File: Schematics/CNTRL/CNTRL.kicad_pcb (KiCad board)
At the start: 4 copper layers, 78 x 78 mm, 128 parts, among them J1 SWD, J10 Y+, J11 Y-, J12 693071020811, J13 3.3V, J14 NAV I2C, J15 I2C, J16 USART, J17 PYRO1_OSTTE020104, J18 PYRO3_OSTTE020104, J19 USB_A_TE_292303-7_Horizontal, J2 CONSMA001-SMD-G-T, J20 PYRO2_OSTTE020104, J21 PYRO4_OSTTE020104, J3 3S LiPo, J4 F4, J5 F3, J6 F2, J7 F1, J8 X+, J9 X-, Q1 BUK9832-55A_CUX, Q2 BUK9832-55A_CUX, Q3 BUK9832-55A_CUX, Q4 BUK9832-55A_CUX, Q5 MMBT2222A-TP, SW1 OS102011MS2QN1, SW2 Omron_B3F-10xx, U1 STM32405RGT6, U2 RFM95W-915S2, U3 TPS2117DRLR, U4 TPS563200, U5 AMS1117-3.3, U6 AMS1117-5.0, U7 W25Q128JVSIQ, U8 USBLC6-2SC6, Y1 12MHz_ECS-120-18-33-JGN-TR3, Y2 32.768KHz_SC32S-7PF20PPM

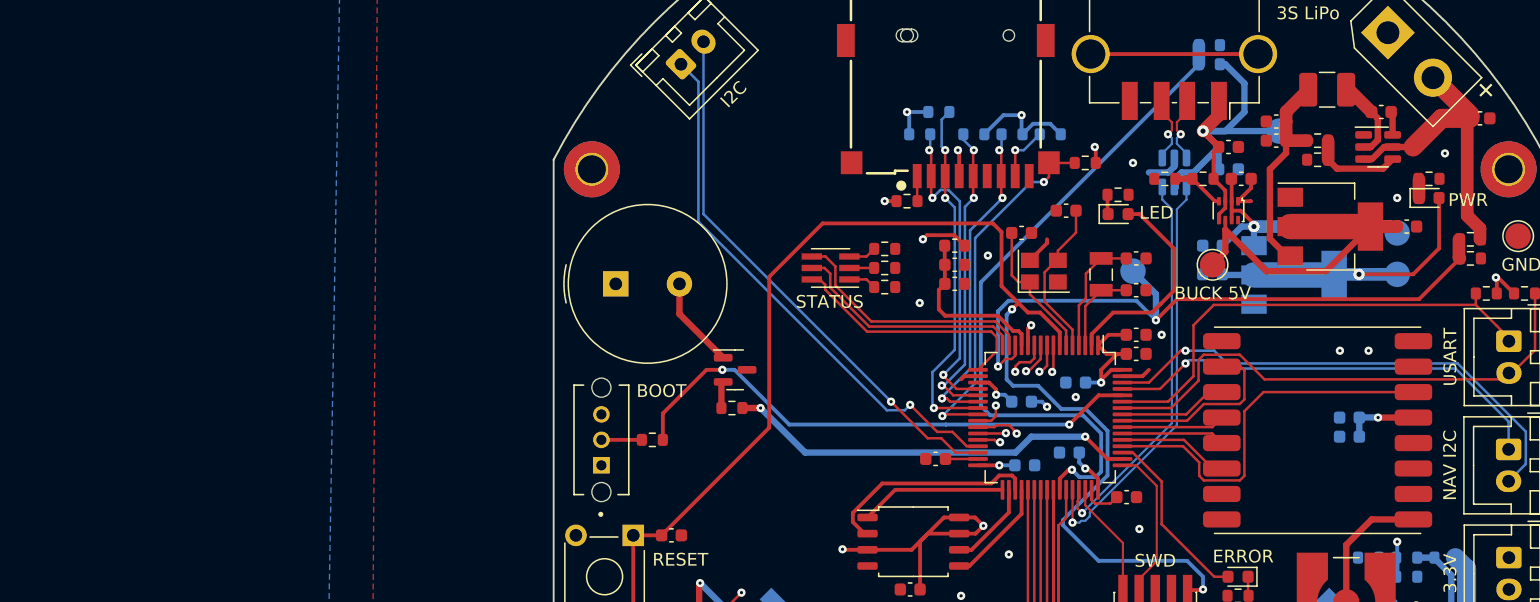
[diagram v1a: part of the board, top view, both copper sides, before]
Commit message: NAVIG v1 fixes and some experimental CNTRL updates for v2
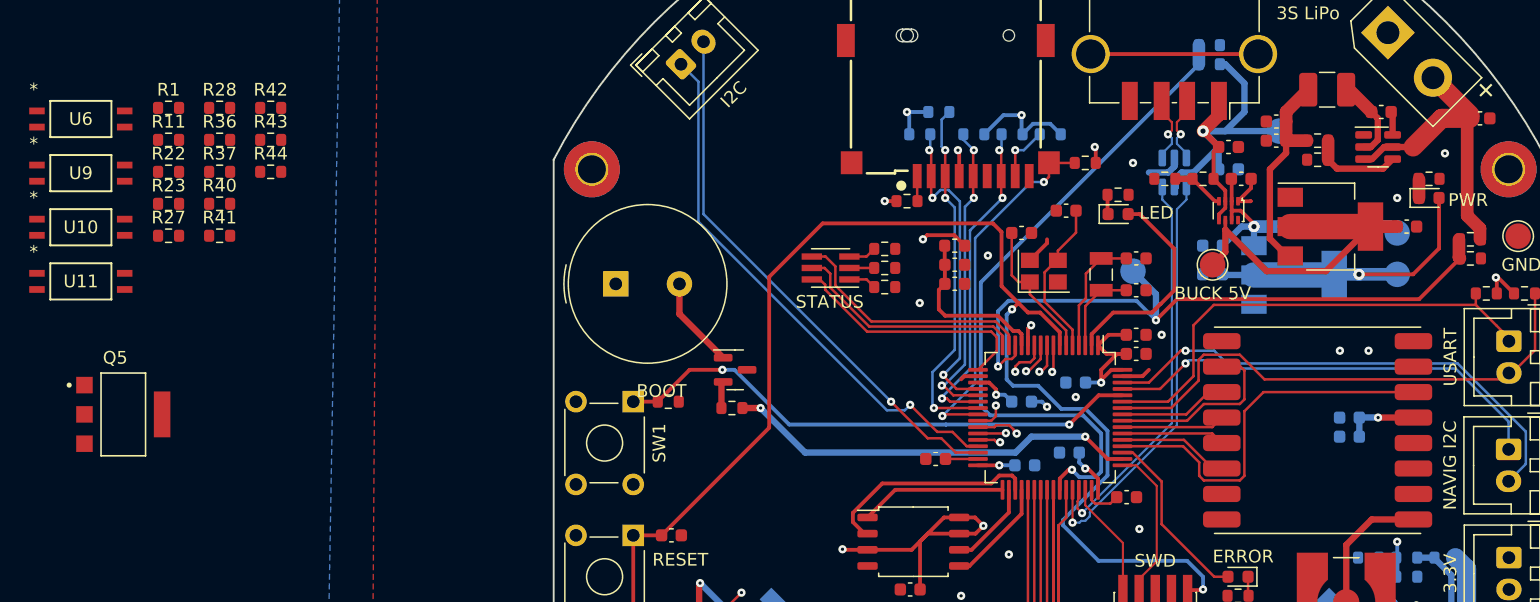
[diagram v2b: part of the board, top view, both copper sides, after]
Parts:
- added Q5: BUK9832-55A_CUX, BUK9832-55A_CUX:TRANS_BUK9832-55A_CUX, F.Cu at (44.2, 89.8)
- added R1: 100K, Resistor_SMD:R_0603_1608Metric, F.Cu at (47.8, 65.7)
- added R11: 10K, Resistor_SMD:R_0603_1608Metric, F.Cu at (47.8, 68.2)
- added R22: 10K, Resistor_SMD:R_0603_1608Metric, F.Cu at (47.8, 70.7)
- added R23: 10K, Resistor_SMD:R_0603_1608Metric, F.Cu at (47.8, 73.2)
- added R27: 10K, Resistor_SMD:R_0603_1608Metric, F.Cu at (47.8, 75.7)
- added R28: 68, Resistor_SMD:R_0603_1608Metric, F.Cu at (51.8, 65.7)
- added R36: 10K, Resistor_SMD:R_0603_1608Metric, F.Cu at (51.8, 68.2)
- added R37: 68, Resistor_SMD:R_0603_1608Metric, F.Cu at (51.8, 70.7)
- added R40: 10K, Resistor_SMD:R_0603_1608Metric, F.Cu at (51.8, 73.2)
- added R41: 68, Resistor_SMD:R_0603_1608Metric, F.Cu at (51.8, 75.7)
- added R42: 10K, Resistor_SMD:R_0603_1608Metric, F.Cu at (55.8, 65.7)
- added R43: 68, Resistor_SMD:R_0603_1608Metric, F.Cu at (55.8, 68.2)
- added R44: 10K, Resistor_SMD:R_0603_1608Metric, F.Cu at (55.8, 70.7)
- added U10: TLP293GB-TPL_E, External:SO4_TOS, F.Cu at (40.9, 75.1)
- added U11: TLP293GB-TPL_E, External:SO4_TOS, F.Cu at (40.9, 79.3)
- added U6: TLP293GB-TPL_E, External:SO4_TOS, F.Cu at (40.9, 66.6)
- added U9: TLP293GB-TPL_E, External:SO4_TOS, F.Cu at (40.9, 70.8)
- J14: value NAV I2C -> NAVIG I2C
- R12: value 100K -> 10K
- SW1: value OS102011MS2QN1 -> Omron_B3F-10xx; footprint External:SW_OS102011MS2QN1 -> Button_Switch_THT:SW_TH_Tactile_Omron_B3F-10xx
- moved SW1 3.91 mm to (84.2, 88.8), turned to -90 degrees
- moved R1 3.25 mm to (87.0, 88.8), turned to 0 degrees
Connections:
- C22 pad 1: Net-(U6-VI) -> BUCK_+5V
- L2 pad 2: Net-(U6-VI) -> BUCK_+5V
- R13 pad 1: Net-(U6-VI) -> BUCK_+5V
- R31 pad 1: Net-(Q5-B) -> Net-(Q5-Pad1)
- SW1 pad 1: GND -> BOOT0
- SW1 pad 2: Net-(SW1-B) -> +3.3V
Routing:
- net Net-(SW1-B): track 3.17 -> 0.00 mm

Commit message: slight fixes to navig board for final production run
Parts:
- removed C24, C26: 10uF, Capacitor_SMD:C_0603_1608Metric
- removed the Q5 at (92.2, 86.2)
- removed the R1 at (87.0, 88.8)
- removed the R11 at (154.2, 80.2)
- removed the R22 at (90.2, 106.0)
- removed the R23 at (136.0, 112.8)
- removed the R27 at (90.2, 107.5)
- removed the R28 at (136.0, 114.2)
- removed the R36 at (97.8, 112.8)
- removed the R37 at (145.0, 101.0)
- removed the R40 at (97.8, 114.2)
- removed the R41 at (145.0, 102.5)
- removed the U6 at (139.0, 75.0)
- moved Q5 50.1 mm to (94.2, 87.8)
- moved R31 3.91 mm to (89.5, 92.2)
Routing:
- net Net-(U6-VI): track 16.8 -> 0.00 mm
- net Net-(Q5-Pad1): track 0.00 -> 7.85 mm
- net USART1_TX: track 41.3 -> 33.6 mm
- net BUCK_+5V: track 26.5 -> 21.7 mm
- net PYRO_2_SENSE: track 44.5 -> 40.7 mm, vias 2 -> 1
- net Net-(BZ1-+): track 7.22 -> 10.9 mm
- net PYRO_1_SENSE: track 41.7 -> 38.7 mm
- net PYRO_3_SENSE: track 47.3 -> 44.5 mm
- net Net-(Q5-B): track 2.11 -> 0.00 mm
- net +3.3V: track 99.4 -> 97.6 mm
- net PYRO_4_SENSE: track 39.1 -> 37.6 mm
- net BUZZER: track 32.5 -> 33.8 mm
- net GND: track 15.0 -> 14.0 mm
